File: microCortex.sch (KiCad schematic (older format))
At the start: 31 parts, among them J1 Feather, J2 20021121-00010C4LF, SW1 KMR231NG LFS, U1 ATSAMD21G18A-AUT, U2 BQ24075, U3 BQ27441DRZR-G1A, U4 TLV70033_WSON6, U5 BMP280, Y1 Crystal

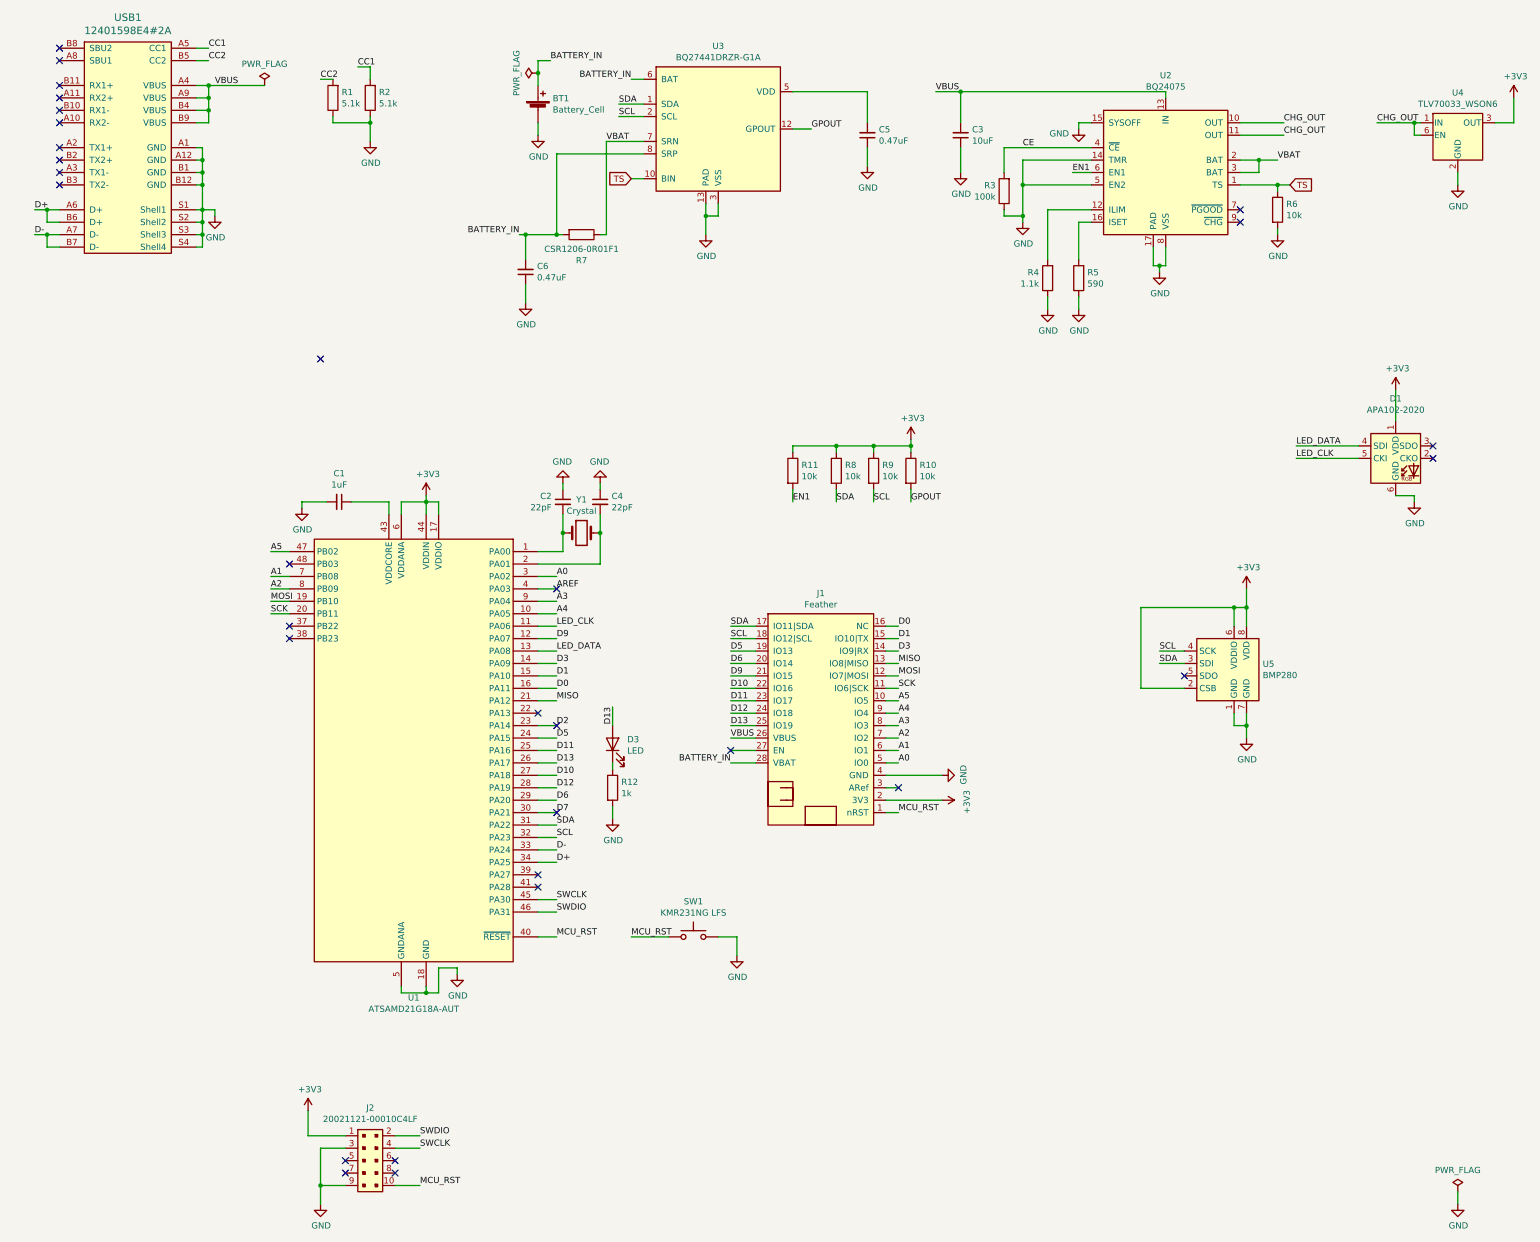
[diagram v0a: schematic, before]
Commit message: Upload PDF & add pin numbers
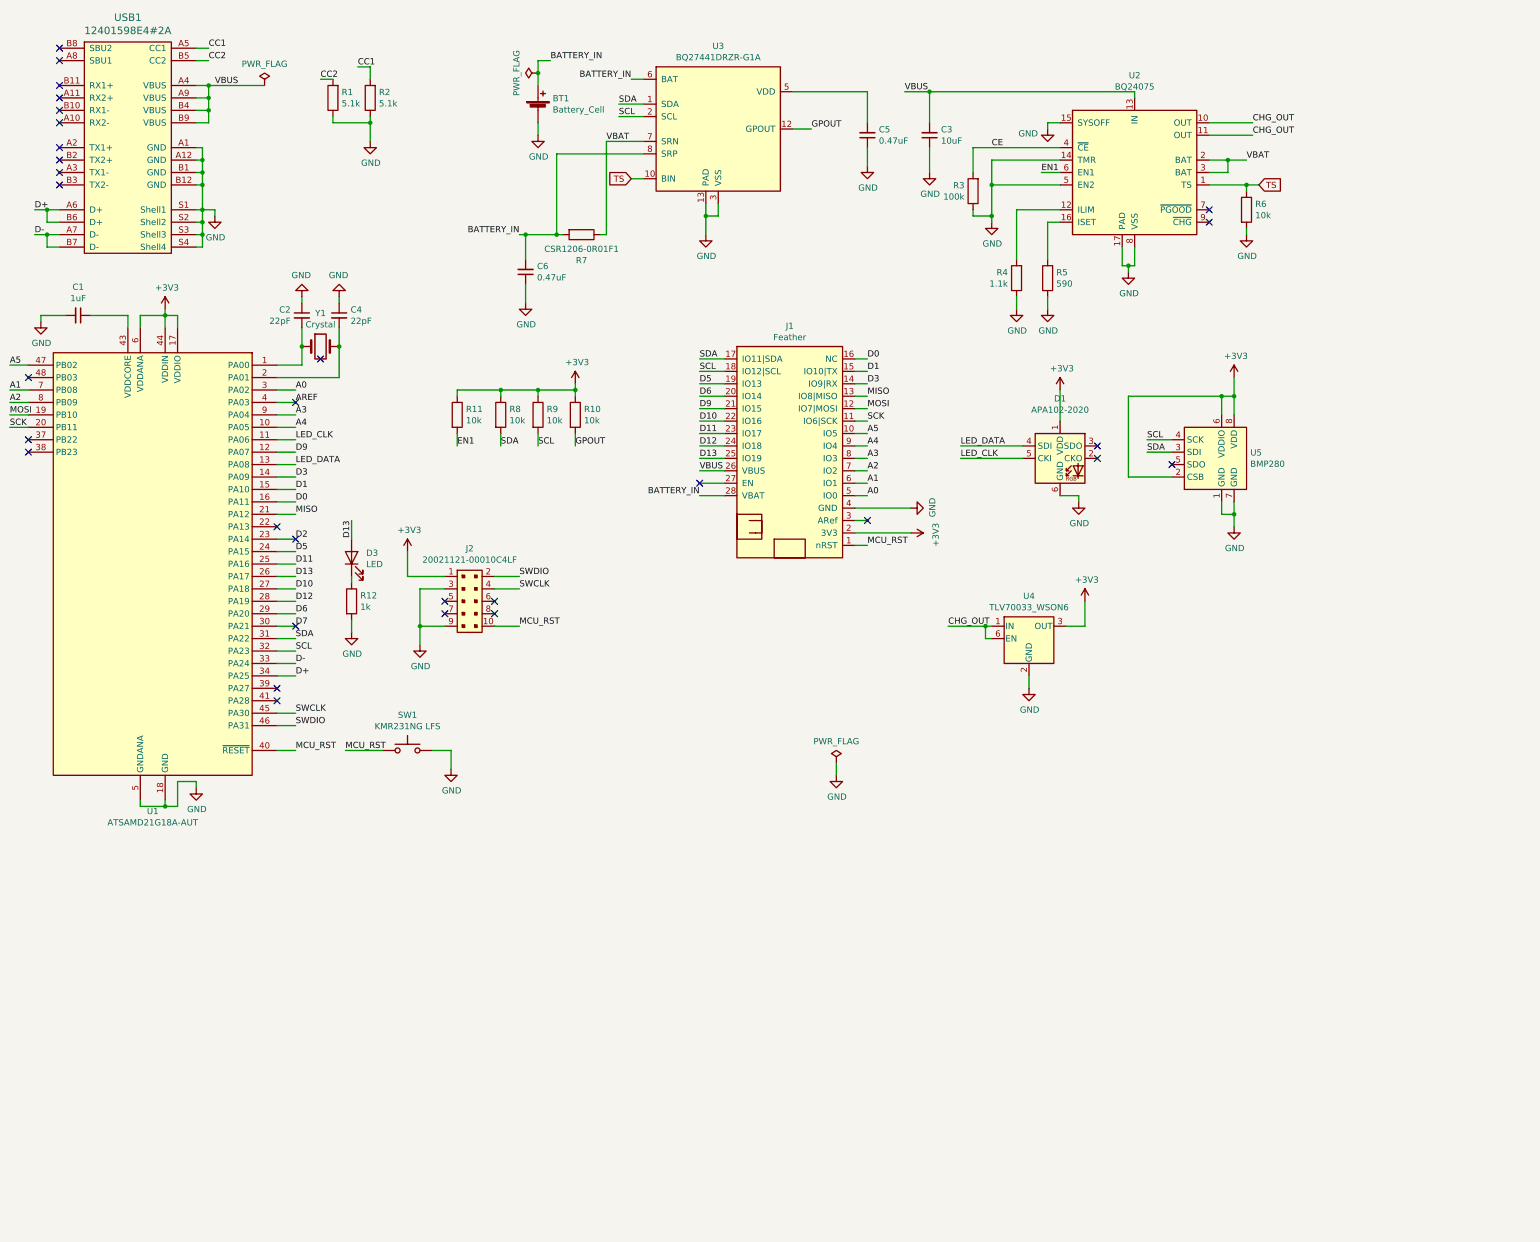
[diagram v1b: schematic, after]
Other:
- moved on the sheet: C1, C2, C3, C4, D1, D3, J1, J2, R10, R11, R12, R3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
